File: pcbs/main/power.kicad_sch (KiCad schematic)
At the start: 4 parts, among them J3 B2B-XH-A, J4 XT30PW-M

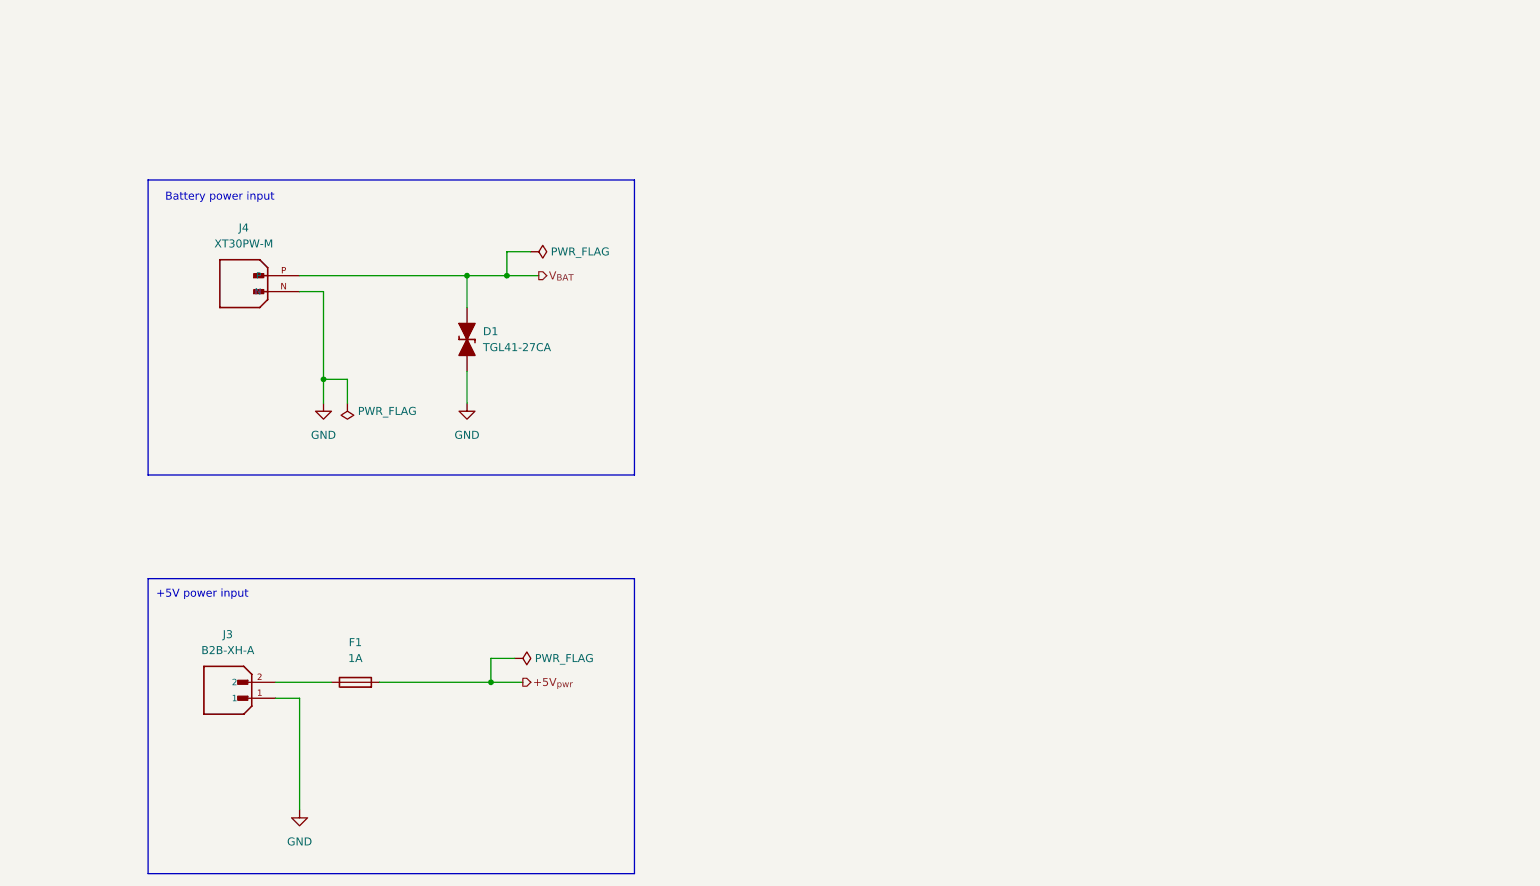
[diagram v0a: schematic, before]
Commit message: First version with 12x8 cm proofboard.
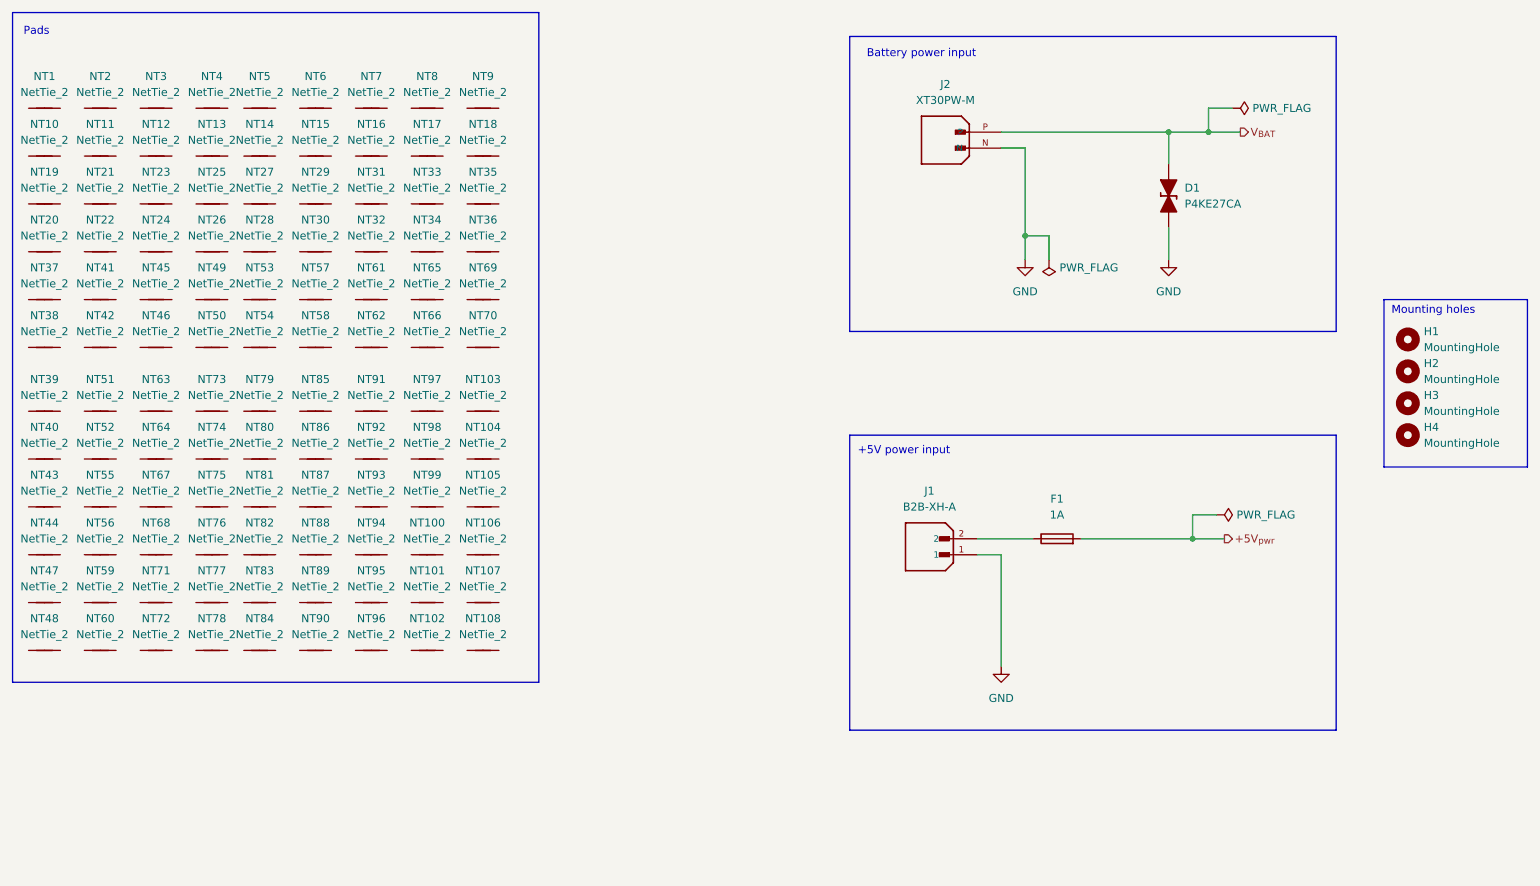
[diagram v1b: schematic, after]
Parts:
- removed D1: TGL41-27CA, PCM_Diode_SMD_AKL:D_MELF_TVS, symbol PCM_Diode_TVS_AKL:TGL41-27CA
- added D1: P4KE27CA, PCM_Diode_THT_AKL:D_DO-41_SOD81_P7.62mm_Horizontal_TVS, symbol PCM_Diode_TVS_AKL:P4KE27CA
- added H1, H2, H3, H4: MountingHole, MountingHole:MountingHole_2.5mm_Pad_TopBottom, symbol Mechanical:MountingHole
- added NT1, NT10, NT100, NT101, NT102, NT103, NT104, NT105, NT106, NT107, NT108, NT11, NT12, NT13, NT14, NT15, NT16, NT17, NT18, NT19, NT2, NT20, NT21, NT22, NT23, NT24, NT25, NT26, NT27, NT28, NT29, NT3, NT30, NT31, NT32, NT33, NT34, NT35, NT36, NT37, NT38, NT39, NT4, NT40, NT41, NT42, NT43, NT44, NT45, NT46, NT47, NT48, NT49, NT5, NT50, NT51, NT52, NT53, NT54, NT55, NT56, NT57, NT58, NT59, NT6, NT60, NT61, NT62, NT63, NT64, NT65, NT66, NT67, NT68, NT69, NT7, NT70, NT71, NT72, NT73, NT74, NT75, NT76, NT77, NT78, NT79, NT8, NT80, NT81, NT82, NT83, NT84, NT85, NT86, NT87, NT88, NT89, NT9, NT90, NT91, NT92, NT93, NT94, NT95, NT96, NT97, NT98, NT99: NetTie_2, NetTie:NetTie-2_SMD_Pad2.0mm, symbol Device:NetTie_2
- renumbered J3 to J1, J4 to J2
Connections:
- net GND: now also D1.1 (K)
- net V_{BAT}: now also D1.2 (A)
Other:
- note added: "Mounting holes"
- note added: "Pads"
- moved on the sheet: F1, J1, J2
